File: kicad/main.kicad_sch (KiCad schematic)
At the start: 34 parts, among them J1 Barrel_Jack, SW1 Reset, U1 KM1810VM88, U10 L7805, U11 15 MHz, U18 1.8432 MHz, U2 W27C512, U3 AS6C4008-55PCN, U4 74HC573, U5 74HC573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

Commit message: Add 8259 interrupt controller, update PCB
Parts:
- removed C13: 0.1 uF, footprints:C_Disc_Long, symbol Device:C
- added unit 5 of U8
- added unit 4 of U8
- added unit 6 of U8
- C12: footprint footprints:C_Disc_Long -> footprints:C_Disc_VeryLong
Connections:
- net INT~{EN}: now reaches U6.18 (I/O/Q)
- no-connect marks 20 -> 25
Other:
- note added: "Address decoder"
- note added: "Clocks"
- note removed: "Address decoder & clock"
- moved on the sheet: U6, U8A, U8B

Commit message: 135x160 board
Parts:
- removed J3: ~, Connector_PinHeader_2.54mm:PinHeader_1x02_P2.54mm_Vertical, symbol Connector:Conn_01x02_Pin
- removed RN1: 5K, Resistor_THT:R_Array_SIP5, symbol Device:R_Network04_Split
- added C13: 0.1 uF, footprints:C_Disc_VeryLong, symbol Device:C
- added RN1: R_Network03_Split, Resistor_THT:R_Array_SIP4, symbol Device:R_Network03_Split
- added SW2: SW_Push_DPDT, footprints:PB22E06, symbol my:SW_Push_DPDT_R
- added U15: AS6C4008-55PCN, Package_DIP:DIP-32_W15.24mm, symbol Memory_RAM:AS6C4008-55PCN
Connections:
- net +5V: now also C13.1, RN1.1 (R1), RN1.1 (R1), RN1.1 (R1), U15.32 (VCC)
- net AD_{0}: now also U15.13 (DQ0)
- net AD_{1}: now also U15.14 (DQ1)
- net AD_{2}: now also U15.15 (DQ2)
- net AD_{3}: now also U15.17 (DQ3)
- net AD_{4}: now also U15.18 (DQ4)
- net AD_{5}: now also U15.19 (DQ5)
- net AD_{6}: now also U15.20 (DQ6)
- net AD_{7}: now also U15.21 (DQ7)
- net A_{0}: now also U15.12 (A0)
- net A_{10}: now also U15.23 (A10)
- net A_{11}: now also U15.25 (A11)
- net A_{12}: now also U15.4 (A12)
- net A_{13}: now also U15.28 (A13)
- net A_{14}: now also U15.3 (A14)
- net A_{15}: now also U15.31 (A15)
- net A_{16}: now also U15.2 (A16)
- net A_{17}: now also U15.30 (A17)
- net A_{18}: now also U15.1 (A18)
- net A_{1}: now also U15.11 (A1)
- net A_{2}: now also U15.10 (A2)
- net A_{3}: now also U15.9 (A3)
- net A_{4}: now also U15.8 (A4)
- net A_{5}: now also U6.2 (I), U15.7 (A5)
- net A_{6}: now also U6.3 (I), U15.6 (A6)
- net A_{7}: now also U15.5 (A7)
- net A_{8}: now also U15.27 (A8); no longer U6.2 (I)
- net A_{9}: now also U15.26 (A9); no longer U6.3 (I)
- net CLK: now also U8.4; no longer U8.2
- net GND: now also C13.2, SW2.3 (C), U15.16 (VSS); no longer J1.2
- net INT~{EN}: now also U6.17 (I/O/Q); no longer U6.18 (I/O/Q)
- net ROM~{EN}: now also U6.16 (I/O/Q); no longer U6.23 (I/O/Q)
- net TIMERCLK: now also U8.2; no longer U8.4
- net TIMER~{EN}: now also U6.19 (I/O/Q); no longer U6.20 (I/O/Q)
- net UART~{EN}: now also U6.18 (I/O/Q); no longer U6.19 (I/O/Q)
- net ~{RD}: now also U15.24 (OE#)
- net ~{WR}: now also U15.29 (WE#)
- net at U10.1 (IN): now also SW2.6 (C)
- net at J1.1: now also SW2.5 (B)
- net at U1.22 (READY): now also RN1.2 (R1.2)
- net at U8.3: now also U6.22 (I/O/Q); no longer U6.16 (I/O/Q)
- net HIRAM~{EN}: now reaches U6.14 (I/O/Q)
- net HIRAM~{EN}: now also U15.22 (CE#)
- net at U8.1: now also U6.23 (I/O/Q); no longer U6.15 (I/O/Q)
- net at U1.17 (NMI): now also RN1.3 (R2.2)
- net at U1.33 (MN/~{MX}): now also RN1.4 (R3.2)
- net IO~{EN}: no longer names the net of U6.21 (I/O/Q)
- net RAM~{EN} renamed LORAM~{EN}
- net LORAM~{EN}: now also U6.15 (I/O/Q); no longer U6.22 (I/O/Q)
- new net: J1.2, SW2.2 (B)
- new net PPI~{EN}: U6.20 (I/O/Q)
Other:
- moved on the sheet: C1, D1, D2, J1, R2, R3, SW1, U10, U2, U3, U6, U7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

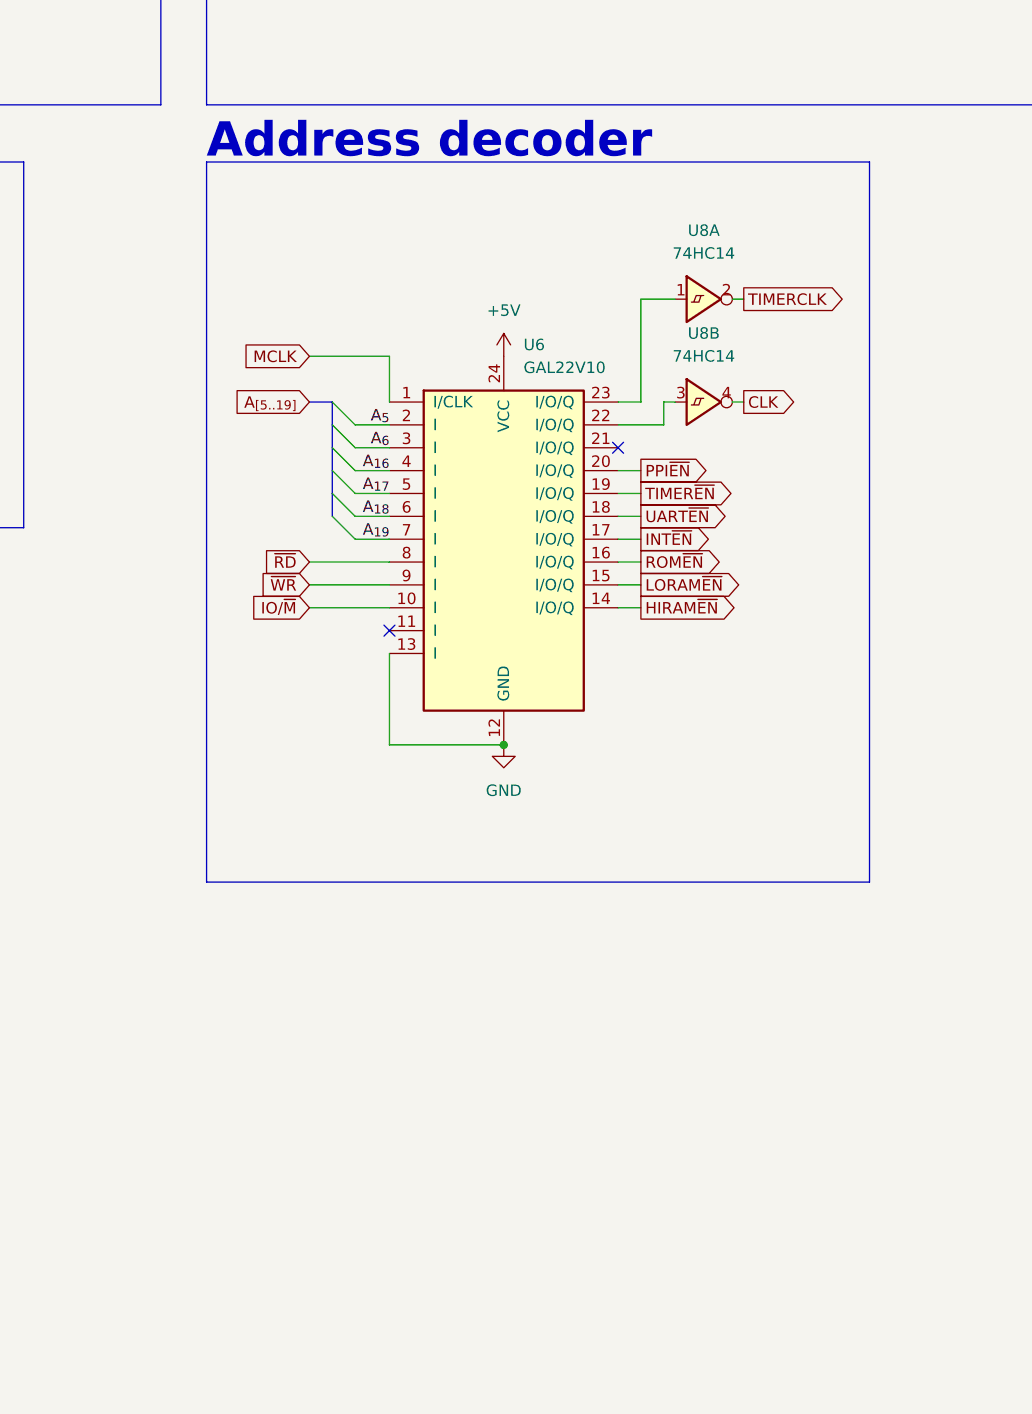
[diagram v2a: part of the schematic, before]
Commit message: Add second GAL
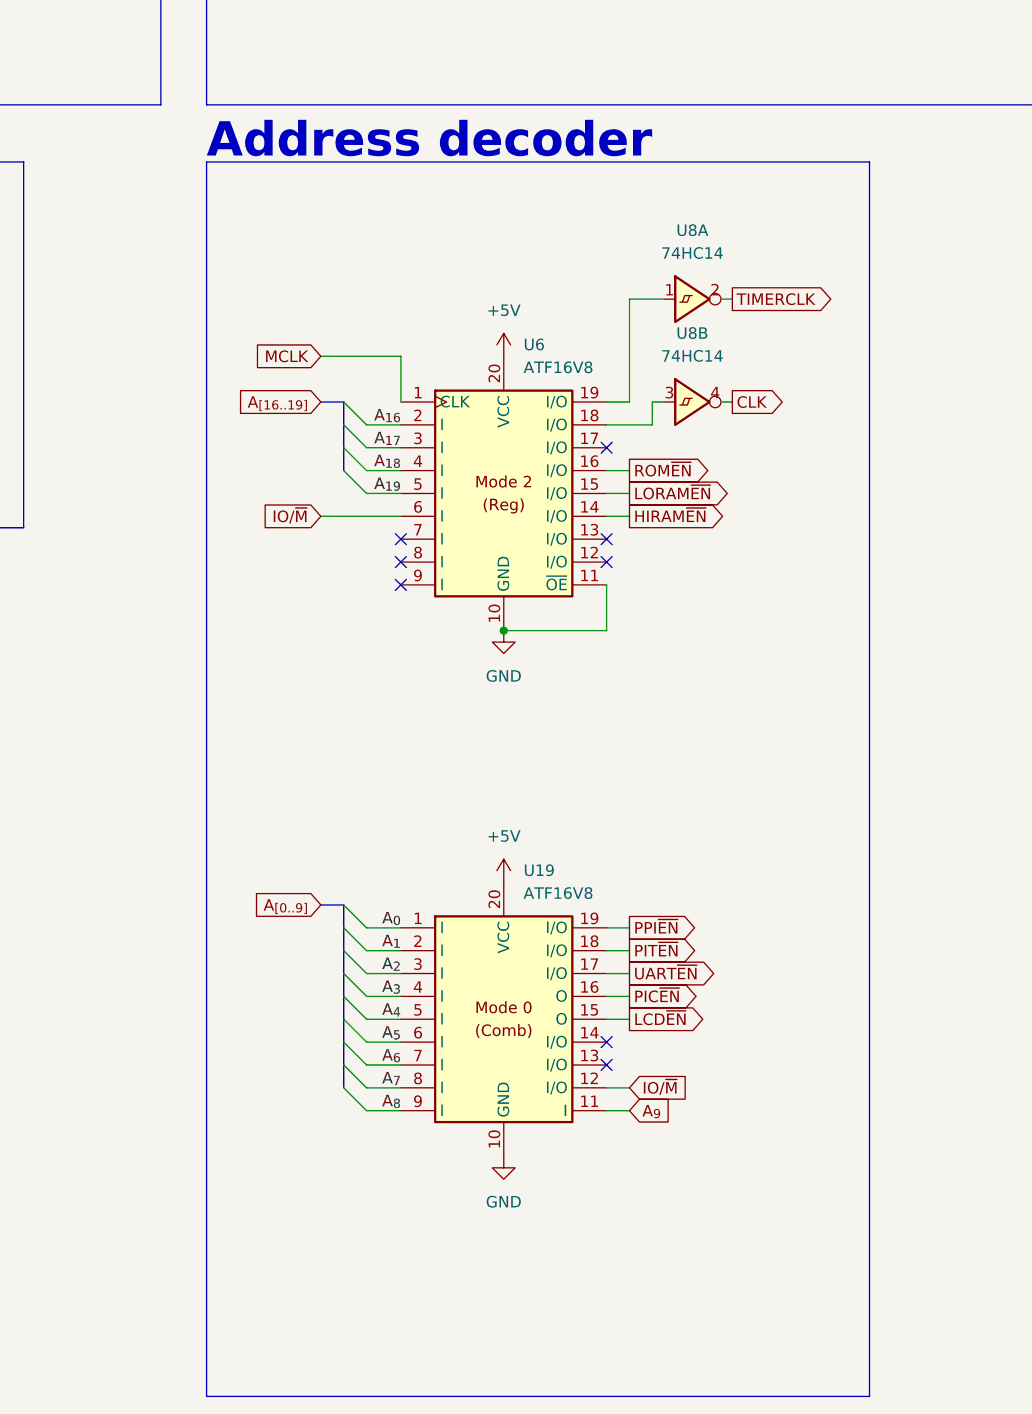
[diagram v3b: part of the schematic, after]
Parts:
- removed U6: GAL22V10, Package_DIP:DIP-24_W7.62mm_Socket, symbol my:GAL22V10
- added U19: ATF16V8, Package_DIP:DIP-20_W7.62mm_Socket, symbol my:ATF16V8_Mode0
- added U6: ATF16V8, Package_DIP:DIP-20_W7.62mm_Socket, symbol my:ATF16V8_Mode2
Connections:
- net +5V: now also U19.20 (VCC), U6.20 (VCC)
- net A_{0}: now also U19.1 (I)
- net A_{16}: now also U6.2 (I)
- net A_{17}: now also U6.3 (I)
- net A_{18}: now also U6.4 (I)
- net A_{19}: now also U6.5 (I)
- net A_{1}: now also U19.2 (I)
- net A_{2}: now also U19.3 (I)
- net A_{3}: now also U19.4 (I)
- net A_{4}: now also U19.5 (I)
- net A_{5}: now also U19.6 (I)
- net A_{6}: now also U19.7 (I)
- net A_{7}: now also U19.8 (I)
- net A_{8}: now also U19.9 (I)
- net A_{9}: now also U19.11 (I)
- net GND: now also U19.10 (GND), U6.10 (GND), U6.11 (~{OE})
- net HIRAM~{EN}: now also U6.14 (I/O)
- net IO/~{M}: now also U19.12 (I/O), U6.6 (I)
- net LORAM~{EN}: now also U6.15 (I/O)
- net MCLK: now also U6.1 (CLK)
- net PPI~{EN}: now also U19.19 (I/O)
- net ROM~{EN}: now also U6.16 (I/O)
- net UART~{EN}: now also U19.17 (I/O)
- net at U8.3: now also U6.18 (I/O)
- net at U8.1: now also U6.19 (I/O)
- new net LCD~{EN}: U19.15 (O)
- new net PIC~{EN}: U19.16 (O)
- new net PIT~{EN}: U19.18 (I/O)
- no-connect marks 25 -> 31
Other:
- moved on the sheet: U8A, U8B

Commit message: PCB 2.0 RC
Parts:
- added C1: 0.1 uF, footprints:C_Disc_Long, symbol Device:C
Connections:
- net +5V: now also C1.1
- net A_{0}: now also U19.9 (I); no longer U19.1 (I)
- net A_{1}: now also U19.8 (I); no longer U19.2 (I)
- net A_{2}: now also U19.7 (I); no longer U19.3 (I)
- net A_{3}: now also U19.6 (I); no longer U19.4 (I)
- net A_{5}: now also U19.4 (I); no longer U19.6 (I)
- net A_{6}: now also U19.3 (I); no longer U19.7 (I)
- net A_{7}: now also U19.2 (I); no longer U19.8 (I)
- net A_{8}: now also U19.1 (I); no longer U19.9 (I)
- net GND: now also C1.2
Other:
- moved on the sheet: C10, C11, C12, C13, C2, C3, C4, C5, C6, C7, C8, C9

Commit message: Cleaner PCB
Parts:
- H1, H2: footprint footprints:Hole_2.5x4 -> footprints:Hole_3.5x5
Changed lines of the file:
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@@
       (effects (font (size 1.27 1.27)) (justify left))
     )
-    (property "Footprint" "footprints:Hole_2.5x4" (at 56.515 248.92 0)
+    (property "Footprint" "footprints:Hole_3.5x5" (at 56.515 248.92 0)
       (effects (font (size 1.27 1.27)) hide)
     )
@@
       (effects (font (size 1.27 1.27)) (justify left))
     )
-    (property "Footprint" "footprints:Hole_2.5x4" (at 27.305 248.92 0)
-      (effects (font (size 1.27 1.27)) hide)
-    )
+    (property "Footprint" "footprints:Hole_3.5x5" (at 27.305 248.92 0)
+      (effects (font (size 1.27 1.27)) hide)
+    )

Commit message: Final PCB
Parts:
- U15: value AS6C4008-55PCN -> RAM2 (AS6C4008)
- U2: value W27C512 -> ROM (W27C512)
- U3: value AS6C4008-55PCN -> RAM1 (AS6C4008)
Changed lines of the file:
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@@
       (effects (font (size 1.27 1.27)) (justify left))
     )
-    (property "Value" "W27C512" (at 238.4141 48.26 0)
+    (property "Value" "ROM (W27C512)" (at 238.4141 48.26 0)
       (effects (font (size 1.27 1.27)) (justify left))
     )
@@
       (effects (font (size 1.27 1.27)) (justify left))
     )
-    (property "Value" "AS6C4008-55PCN" (at 299.3741 48.26 0)
+    (property "Value" "RAM1 (AS6C4008)" (at 299.3741 48.26 0)
       (effects (font (size 1.27 1.27)) (justify left))
     )
@@
       (effects (font (size 1.27 1.27)) (justify left))
     )
-    (property "Value" "AS6C4008-55PCN" (at 365.4141 48.26 0)
-      (effects (font (size 1.27 1.27)) (justify left))
-    )
+    (property "Value" "RAM2 (AS6C4008)" (at 365.4141 48.26 0)
+      (effects (font (size 1.27 1.27)) (justify left))
+    )

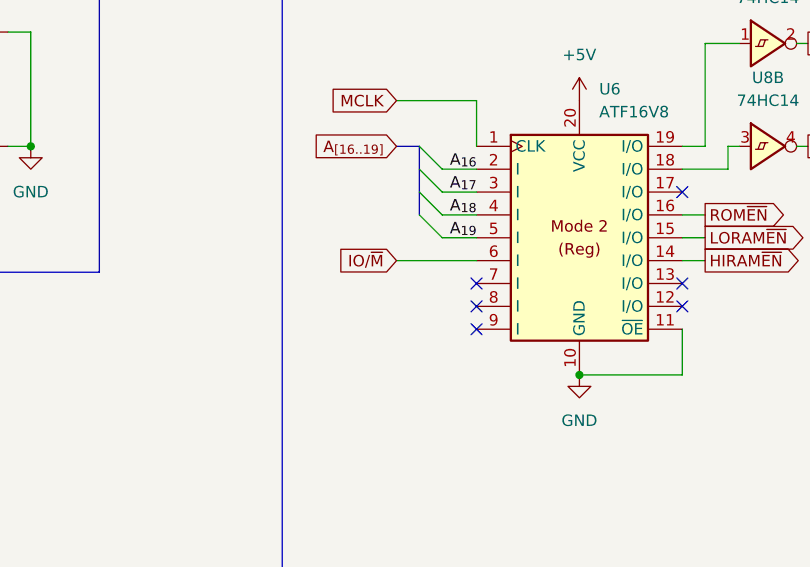
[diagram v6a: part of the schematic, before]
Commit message: New PCB (add MCB line)
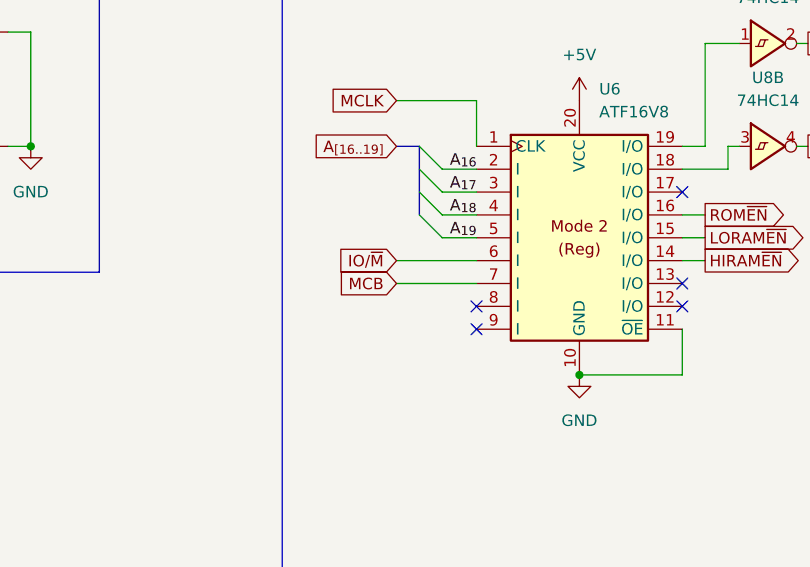
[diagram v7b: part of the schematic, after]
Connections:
- net MCB: now reaches U6.7 (I)
- no-connect marks 31 -> 30
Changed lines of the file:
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@@
   (no_connect (at 27.94 208.28))
   (no_connect (at 386.08 227.33))
-  (no_connect (at 223.52 182.88))
   (no_connect (at 26.67 167.64))
   (no_connect (at 246.38 185.42))
@@
     (stroke (width 0) (type default))
   )
+  (wire (pts (xy 214.63 182.88) (xy 223.52 182.88))
+    (stroke (width 0) (type default))
+  )
   (wire (pts (xy 45.72 210.82) (xy 43.18 210.82))
     (stroke (width 0) (type default))
@@
       (effects (font (size 1.27 1.27)) (justify right) hide)
     )
+  )
+  (global_label "MCB" (shape input) (at 214.63 182.88 180) (fields_autoplaced)
+    (effects (font (size 1.27 1.27)) (justify right))
+    (property "Intersheetrefs" "${INTERSHEET_REFS}" (at 207.6534 182.88 0)
+      (effects (font (size 1.27 1.27)) (justify right) hide)
+    )

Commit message: V0.3 WIP
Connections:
- net PS2~{EN}: now reaches U19.14 (I/O)
- net SPKROUT: now reaches U6.12 (I/O)
- net T2OUT: now reaches U6.8 (I)
- net SPKREN: now reaches U6.9 (I)
- no-connect marks 30 -> 26
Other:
- note added: "Address & port decoder"
- note removed: "Address decoder"
- moved on the sheet: U19, U6, U8A, U8B
